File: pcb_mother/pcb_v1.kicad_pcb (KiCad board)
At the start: 2 copper layers, 90 x 70.2 mm, 27 parts, among them J1 Conn_01x02, J10 Conn_01x02, J11 Conn_01x06, J14 Conn_01x06, J2 Conn_01x03, J3 Conn_01x02, J4 Conn_01x02_Male, J5 Conn_01x02_Male, J9 Conn_01x02, Q10 2N2219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

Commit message: falta agregar el plano de tierra y los aujeros, comprobar todo. Ver tutoriales de tutoelectro (el gallego)
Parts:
- moved REF** 121.2 mm to (196.7, 39.1)
- moved REF** 83.5 mm to (185.2, 137.7)
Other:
- board size 90 x 70.2 mm -> 80 x 90 mm
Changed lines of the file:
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@@
     (links 104)
     (no_connects 0)
-    (area 68.724999 51.924999 158.875001 122.275001)
+    (area 72.632999 32.841 210.279286 136.365619)
     (thickness 1.6)
-    (drawings 3)
+    (drawings 6)
     (tracks 398)
     (zones 0)
@@
   )
   (module Mounting_Holes:MountingHole_4mm (layer F.Cu)
-    (at 77.6605 61.976)
+    (at 196.723 39.116)
     (descr "Mounting Hole 4mm, no annular")
     (tags "mounting hole 4mm no annular")
@@
   )
   (module Mounting_Holes:MountingHole_4mm (layer F.Cu)
-    (at 202.565 56.007)
+    (at 185.166 137.668)
     (descr "Mounting Hole 4mm, no annular")
     (tags "mounting hole 4mm no annular")
@@
     )
   )
+  (gr_line (start 65 50) (end 65 140) (angle 90) (layer Edge.Cuts) (width 0.15))
+  (gr_line (start 145 50) (end 65 50) (angle 90) (layer Edge.Cuts) (width 0.15))
+  (gr_line (start 145 140) (end 145 50) (angle 90) (layer Edge.Cuts) (width 0.15))
+  (gr_line (start 65 140) (end 145 140) (angle 90) (layer Edge.Cuts) (width 0.15))
+  (dimension 82.550391 (width 0.3) (layer F.Fab)
+    (gr_text "82,550 mm" (at 185.039 96.266 270.1762941) (layer F.Fab)
+      (effects (font (size 1.5 1.5) (thickness 0.3)))
+    )
+    (feature1 (pts (xy 185.166 137.541) (xy 185.166 137.541)))
+    (feature2 (pts (xy 184.912 54.991) (xy 184.912 54.991)))
+    (crossbar (pts (xy 184.912 54.991) (xy 185.166 137.541)))
+    (arrow1a (pts (xy 185.166 137.541) (xy 184.576116 136.416306)))
+    (arrow1b (pts (xy 185.166 137.541) (xy 185.748952 136.412697)))
+    (arrow2a (pts (xy 184.912 54.991) (xy 184.329048 56.119303)))
+    (arrow2b (pts (xy 184.912 54.991) (xy 185.501884 56.115694)))
+  )
   (gr_line (start 91.601 103.098) (end 91.401 103.098) (angle 90) (layer Edge.Cuts) (width 0.15))
-  (gr_line (start 158.8 52) (end 68.8 52) (angle 90) (layer Edge.Cuts) (width 0.15))
-  (gr_line (start 158.8 122.2) (end 158.8 52) (angle 90) (layer Edge.Cuts) (width 0.15))
   (segment (start 128.524 112.903) (end 128.524 109.601) (width 0.8) (layer F.Cu) (net 4))
   (segment (start 117.348 98.425) (end 117.348 97.028) (width 0.8) (layer F.Cu) (net 4))
@@
   (segment (start 102.12 81.776) (end 102.108 81.788) (width 0.8) (layer F.Cu) (net 8))
   (segment (start 102.12 81.776) (end 102.108 81.788) (width 0.8) (layer F.Cu) (net 8))
-  (segment (start 99.568 81.788) (end 99.568 82.804) (width 0.8) (layer F.Cu) (net 9) (status C00000))
-  (segment (start 99.568 82.804) (end 98.298 84.074) (width 0.8) (layer F.Cu) (net 9) (status 400000))
-  (segment (start 112.28 74.688) (end 112.28 76.24) (width 0.8) (layer F.Cu) (net 9) (status 800000))
+  (segment (start 99.568 81.788) (end 99.568 82.804) (width 0.8) (layer F.Cu) (net 9))
+  (segment (start 99.568 82.804) (end 98.298 84.074) (width 0.8) (layer F.Cu) (net 9))
+  (segment (start 112.28 74.688) (end 112.28 76.24) (width 0.8) (layer F.Cu) (net 9))
   (segment (start 108.712 71.12) (end 112.28 74.688) (width 0.8) (layer F.Cu) (net 9))
   (segment (start 86.868 71.12) (end 108.712 71.12) (width 0.8) (layer F.Cu) (net 9))
@@
   (segment (start 97.04 81.776) (end 97.028 81.788) (width 0.8) (layer F.Cu) (net 11))
   (segment (start 97.04 81.776) (end 97.028 81.788) (width 0.8) (layer F.Cu) (net 11))
-  (segment (start 107.569 131.318) (end 107.569 132.334) (width 0.8) (layer F.Cu) (net 12) (status 400000))
+  (segment (start 107.569 131.318) (end 107.569 132.334) (width 0.8) (layer F.Cu) (net 12))
   (segment (start 133.731 123.063) (end 133.731 105.283) (width 0.8) (layer F.Cu) (net 12))
   (segment (start 122.936 133.858) (end 133.731 123.063) (width 0.8) (layer F.Cu) (net 12))
@@
   (segment (start 132.6 65.8) (end 132.6 65.6) (width 0.8) (layer F.Cu) (net 12))
   (segment (start 133.7 75.3) (end 133.6 75.2) (width 0.8) (layer F.Cu) (net 12))
-  (segment (start 91.948 81.788) (end 89.154 81.788) (width 0.8) (layer F.Cu) (net 13) (status 400000))
-  (segment (start 96.647 72.517) (end 99.58 75.45) (width 0.8) (layer F.Cu) (net 13) (status 800000))
+  (segment (start 91.948 81.788) (end 89.154 81.788) (width 0.8) (layer F.Cu) (net 13))
+  (segment (start 96.647 72.517) (end 99.58 75.45) (width 0.8) (layer F.Cu) (net 13))
   (segment (start 87.503 72.517) (end 96.647 72.517) (width 0.8) (layer F.Cu) (net 13))
   (segment (start 84.455 75.565) (end 87.503 72.517) (width 0.8) (layer F.Cu) (net 13))
   (segment (start 84.455 77.089) (end 84.455 75.565) (width 0.8) (layer F.Cu) (net 13))
   (segment (start 89.154 81.788) (end 84.455 77.089) (width 0.8) (layer F.Cu) (net 13))
-  (segment (start 99.58 75.45) (end 99.58 76.24) (width 0.8) (layer F.Cu) (net 13) (status C00000))
+  (segment (start 99.58 75.45) (end 99.58 76.24) (width 0.8) (layer F.Cu) (net 13))
   (segment (start 99.58 76.24) (end 99.58 75.38) (width 0.8) (layer F.Cu) (net 13))
   (segment (start 99.58 76.24) (end 99.58 75.98) (width 0.8) (layer F.Cu) (net 13))
@@
   (segment (start 112.268 82.423) (end 112.268 81.788) (width 0.8) (layer F.Cu) (net 36))
   (segment (start 112.268 81.788) (end 112.268 82.169) (width 0.8) (layer F.Cu) (net 36))
-  (segment (start 106.426 109.093) (end 106.807 109.093) (width 0.8) (layer F.Cu) (net 37) (status C00000))
-  (segment (start 106.807 109.093) (end 108.585 107.315) (width 0.8) (layer F.Cu) (net 37) (status 400000))
-  (segment (start 104.648 101.092) (end 104.648 97.028) (width 0.8) (layer F.Cu) (net 37) (status 800000))
+  (segment (start 106.426 109.093) (end 106.807 109.093) (width 0.8) (layer F.Cu) (net 37))
+  (segment (start 106.807 109.093) (end 108.585 107.315) (width 0.8) (layer F.Cu) (net 37))
+  (segment (start 104.648 101.092) (end 104.648 97.028) (width 0.8) (layer F.Cu) (net 37))
   (segment (start 105.41 101.854) (end 104.648 101.092) (width 0.8) (layer F.Cu) (net 37))
   (segment (start 107.188 101.854) (end 105.41 101.854) (width 0.8) (layer F.Cu) (net 37))
@@
   (segment (start 102.108 97.028) (end 102.108 98.171) (width 0.8) (layer F.Cu) (net 38))
   (segment (start 102.108 97.028) (end 102.108 96.908) (width 0.8) (layer F.Cu) (net 38))
-  (segment (start 94.5 76.24) (end 86.574 76.24) (width 0.8) (layer F.Cu) (net 39) (status 400000))
+  (segment (start 94.5 76.24) (end 86.574 76.24) (width 0.8) (layer F.Cu) (net 39))
   (segment (start 86.36 76.454) (end 86.36 83.566) (width 0.8) (layer B.Cu) (net 39))
   (segment (start 86.487 76.327) (end 86.36 76.454) (width 0.8) (layer B.Cu) (net 39))
@@
   (via (at 86.36 98.298) (size 2) (drill 0.75) (layers F.Cu B.Cu) (net 39))
   (segment (start 89.154 101.092) (end 86.36 98.298) (width 0.8) (layer B.Cu) (net 39))
-  (segment (start 114.046 104.013) (end 114.046 103.886) (width 0.8) (layer F.Cu) (net 39) (status C00000))
-  (segment (start 114.046 103.886) (end 111.252 101.092) (width 0.8) (layer F.Cu) (net 39) (status 400000))
+  (segment (start 114.046 104.013) (end 114.046 103.886) (width 0.8) (layer F.Cu) (net 39))
+  (segment (start 114.046 103.886) (end 111.252 101.092) (width 0.8) (layer F.Cu) (net 39))
   (segment (start 100.33 103.378) (end 100.203 103.378) (width 0.8) (layer F.Cu) (net 39))
   (segment (start 102.616 101.092) (end 100.33 103.378) (width 0.8) (layer F.Cu) (net 39))
@@
   (segment (start 111.252 101.092) (end 102.616 101.092) (width 0.8) (layer B.Cu) (net 39))
   (via (at 111.252 101.092) (size 2) (drill 0.75) (layers F.Cu B.Cu) (net 39))
-  (segment (start 124.079 100.203) (end 124.079 101.346) (width 0.8) (layer F.Cu) (net 39) (status C00000))
-  (segment (start 124.079 101.346) (end 132.08 109.347) (width 0.8) (layer F.Cu) (net 39) (status 400000))
-  (segment (start 123.571 131.318) (end 110.109 131.318) (width 0.8) (layer F.Cu) (net 39) (status 800000))
+  (segment (start 124.079 100.203) (end 124.079 101.346) (width 0.8) (layer F.Cu) (net 39))
+  (segment (start 124.079 101.346) (end 132.08 109.347) (width 0.8) (layer F.Cu) (net 39))
+  (segment (start 123.571 131.318) (end 110.109 131.318) (width 0.8) (layer F.Cu) (net 39))
   (segment (start 132.08 122.809) (end 123.571 131.318) (width 0.8) (layer F.Cu) (net 39))
   (segment (start 132.08 109.347) (end 132.08 122.809) (width 0.8) (layer F.Cu) (net 39))
@@
   (segment (start 101.727 103.378) (end 101.727 103.378) (width 0.8) (layer F.Cu) (net 39))
   (segment (start 122.301 127.762) (end 123.825 127.762) (width 0.8) (layer F.Cu) (net 40))
-  (segment (start 119.888 99.06) (end 119.888 97.028) (width 0.8) (layer F.Cu) (net 40) (status 800000))
+  (segment (start 119.888 99.06) (end 119.888 97.028) (width 0.8) (layer F.Cu) (net 40))
   (segment (start 130.683 109.855) (end 119.888 99.06) (width 0.8) (layer F.Cu) (net 40))
   (segment (start 130.683 120.904) (end 130.683 109.855) (width 0.8) (layer F.Cu) (net 40))
@@
   (segment (start 77.089 104.14) (end 77.216 104.14) (width 0.8) (layer F.Cu) (net 43))
   (segment (start 117.348 81.788) (end 117.348 82.169) (width 0.8) (layer F.Cu) (net 43))
-  (segment (start 107.188 97.028) (end 107.188 99.949) (width 0.8) (layer F.Cu) (net 44) (status 400000))
-  (segment (start 109.982 111.633) (end 107.442 114.173) (width 0.8) (layer F.Cu) (net 44) (status 800000))
+  (segment (start 107.188 97.028) (end 107.188 99.949) (width 0.8) (layer F.Cu) (net 44))
+  (segment (start 109.982 111.633) (end 107.442 114.173) (width 0.8) (layer F.Cu) (net 44))
   (segment (start 109.982 102.743) (end 109.982 111.633) (width 0.8) (layer F.Cu) (net 44))
   (segment (start 107.188 99.949) (end 109.982 102.743) (width 0.8) (layer F.Cu) (net 44))
-  (segment (start 107.442 114.173) (end 106.426 114.173) (width 0.8) (layer F.Cu) (net 44) (status C00000))
+  (segment (start 107.442 114.173) (end 106.426 114.173) (width 0.8) (layer F.Cu) (net 44))
   (segment (start 106.426 114.173) (end 106.807 114.173) (width 0.8) (layer F.Cu) (net 44))
   (segment (start 112.268 97.028) (end 112.268 97.409) (width 0.8) (layer F.Cu) (net 45))

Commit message: se realiza un ultimo chekeo antes de la imprecion.
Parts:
- removed the REF** at (196.7, 39.1)
- added REF**: MountingHole_4mm, Mounting_Holes:MountingHole_4mm, F.Cu at (137.4, 131.3)
- added REF**: MountingHole_4mm, Mounting_Holes:MountingHole_4mm, F.Cu at (137.4, 61.3)
- D1: footprint Diodes_SMD:D_1206 -> Diodes_THT:D_DO-35_SOD27_P7.62mm_Horizontal
- moved REF** 112.9 mm to (72.4, 131.3)
- moved REF** 112.7 mm to (72.4, 61.3)
- moved D1 7.27 mm to (136.1, 110.5), turned to 90 degrees
- moved J5 0.30 mm to (84.0, 56.3)
- moved C4 0.20 mm to (88.9, 56.4)
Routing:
- net /Vcc_bat: track 135.0 -> 135.6 mm
- net Net-(D1-Pad2): track 3.69 -> 3.11 mm
- added copper zone on F.Cu, net GND

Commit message: Version final impresa
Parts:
- moved J11 0.92 mm to (110.1, 128.7)
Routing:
- net VCC: track 230.5 -> 233.0 mm
- net /L5_a: track 11.2 -> 12.4 mm
- net /L2_a: track 16.8 -> 17.8 mm
- net /L1_a: track 21.6 -> 22.6 mm
- net /L3_a: track 24.4 -> 25.4 mm
- net /L4_a: track 18.3 -> 19.2 mm

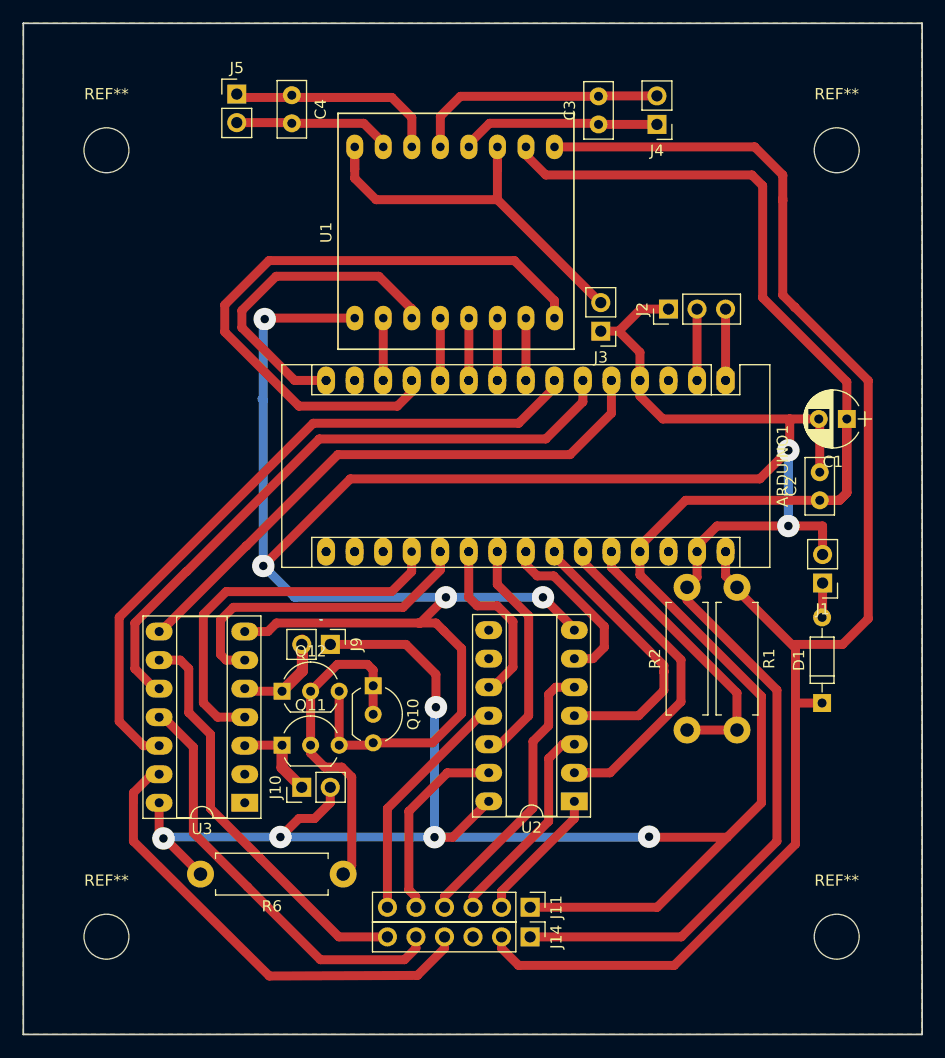
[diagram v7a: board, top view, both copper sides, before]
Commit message: Se modificaron los margenes para que sea igual o a penas mas grande (+2mm). Esta version SI se imprimio, la anterior no, porque era muy grande.
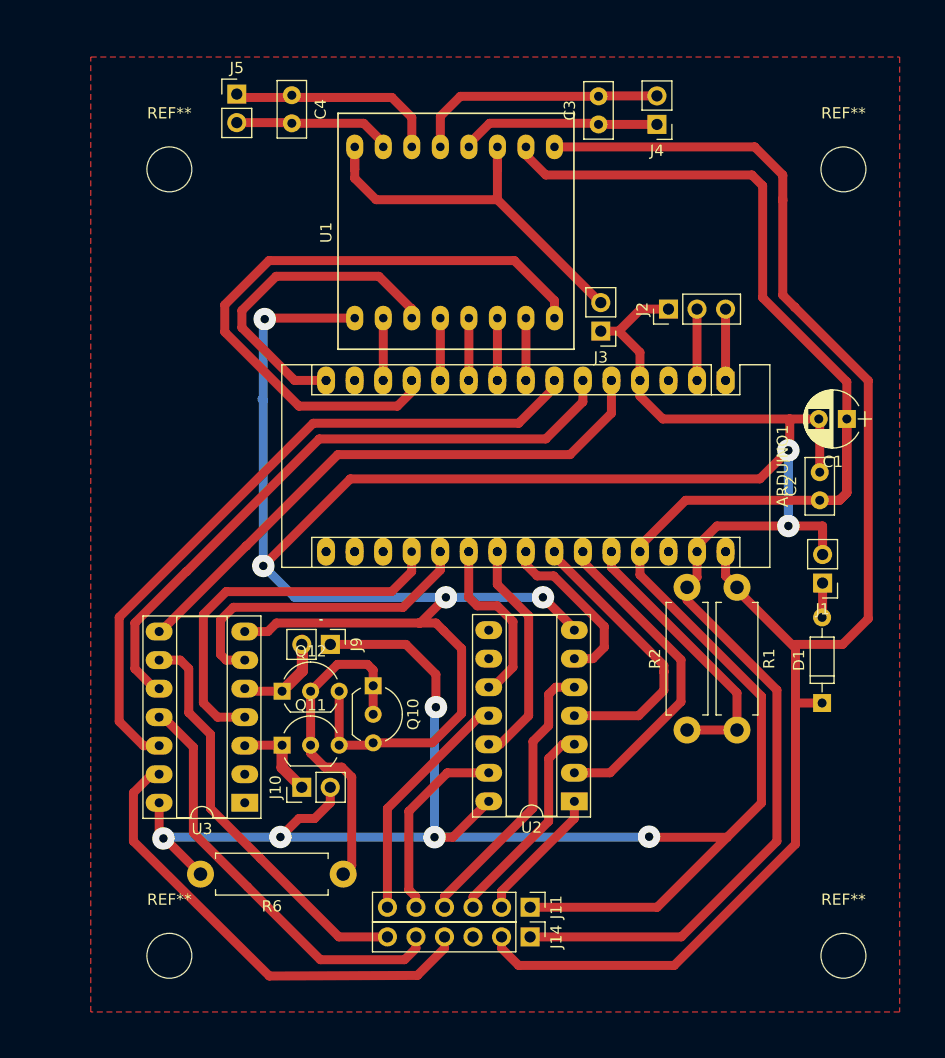
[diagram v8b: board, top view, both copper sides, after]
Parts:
- moved REF** 5.85 mm to (78.0, 63.0)
- moved REF** 5.85 mm to (78.0, 133.0)
- moved REF** 1.80 mm to (138.0, 63.0)
- moved REF** 1.80 mm to (138.0, 133.0)
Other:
- board outline removed
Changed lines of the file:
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@@
     (links 104)
     (no_connects 0)
-    (area 64.685714 27.3 172.85 140.075001)
+    (area 70.285714 43.3 170.85 149.700001)
     (thickness 1.6)
-    (drawings 7)
+    (drawings 14)
     (tracks 417)
     (zones 0)
@@
   )
   (module Mounting_Holes:MountingHole_4mm (layer F.Cu)
-    (at 137.4 131.3)
+    (at 138 133)
     (descr "Mounting Hole 4mm, no annular")
     (tags "mounting hole 4mm no annular")
@@
   )
   (module Mounting_Holes:MountingHole_4mm (layer F.Cu)
-    (at 137.4 61.3)
+    (at 138 63)
     (descr "Mounting Hole 4mm, no annular")
     (tags "mounting hole 4mm no annular")
@@
   )
   (module Mounting_Holes:MountingHole_4mm (layer F.Cu)
-    (at 72.4 61.3)
+    (at 78 63)
     (descr "Mounting Hole 4mm, no annular")
     (tags "mounting hole 4mm no annular")
@@
   )
   (module Mounting_Holes:MountingHole_4mm (layer F.Cu)
-    (at 72.4 131.3)
+    (at 78 133)
     (descr "Mounting Hole 4mm, no annular")
     (tags "mounting hole 4mm no annular")
@@
     )
   )
-  (dimension 80 (width 0.3) (layer F.Fab)
-    (gr_text "80,000 mm" (at 105 28.65) (layer F.Fab)
+  (dimension 72 (width 0.3) (layer F.CrtYd)
+    (gr_text "72,000 mm" (at 107 156.35) (layer F.CrtYd)
       (effects (font (size 1.5 1.5) (thickness 0.3)))
     )
-    (feature1 (pts (xy 65 50) (xy 65 27.3)))
-    (feature2 (pts (xy 145 50) (xy 145 27.3)))
-    (crossbar (pts (xy 145 30) (xy 65 30)))
-    (arrow1a (pts (xy 65 30) (xy 66.126504 29.413579)))
-    (arrow1b (pts (xy 65 30) (xy 66.126504 30.586421)))
-    (arrow2a (pts (xy 145 30) (xy 143.873496 29.413579)))
-    (arrow2b (pts (xy 145 30) (xy 143.873496 30.586421)))
-  )
-  (dimension 90 (width 0.3) (layer F.Fab)
-    (gr_text "90,000 mm" (at 166.35 95 270) (layer F.Fab)
+    (feature1 (pts (xy 143 138) (xy 143 157.7)))
+    (feature2 (pts (xy 71 138) (xy 71 157.7)))
+    (crossbar (pts (xy 71 155) (xy 143 155)))
+    (arrow1a (pts (xy 143 155) (xy 141.873496 155.586421)))
+    (arrow1b (pts (xy 143 155) (xy 141.873496 154.413579)))
+    (arrow2a (pts (xy 71 155) (xy 72.126504 155.586421)))
+    (arrow2b (pts (xy 71 155) (xy 72.126504 154.413579)))
+  )
+  (dimension 85 (width 0.3) (layer Dwgs.User)
+    (gr_text "85,000 mm" (at 164.35 95.5 90) (layer Dwgs.User)
       (effects (font (size 1.5 1.5) (thickness 0.3)))
     )
-    (feature1 (pts (xy 145 140) (xy 167.7 140)))
-    (feature2 (pts (xy 145 50) (xy 167.7 50)))
-    (crossbar (pts (xy 165 50) (xy 165 140)))
-    (arrow1a (pts (xy 165 140) (xy 164.413579 138.873496)))
-    (arrow1b (pts (xy 165 140) (xy 165.586421 138.873496)))
-    (arrow2a (pts (xy 165 50) (xy 164.413579 51.126504)))
-    (arrow2b (pts (xy 165 50) (xy 165.586421 51.126504)))
-  )
-  (gr_line (start 65 50) (end 65 140) (angle 90) (layer Edge.Cuts) (width 0.15))
-  (gr_line (start 145 50) (end 65 50) (angle 90) (layer Edge.Cuts) (width 0.15))
-  (gr_line (start 145 140) (end 145 50) (angle 90) (layer Edge.Cuts) (width 0.15))
-  (gr_line (start 65 140) (end 145 140) (angle 90) (layer Edge.Cuts) (width 0.15))
+    (feature1 (pts (xy 143 53) (xy 165.7 53)))
+    (feature2 (pts (xy 143 138) (xy 165.7 138)))
+    (crossbar (pts (xy 163 138) (xy 163 53)))
+    (arrow1a (pts (xy 163 53) (xy 163.586421 54.126504)))
+    (arrow1b (pts (xy 163 53) (xy 162.413579 54.126504)))
+    (arrow2a (pts (xy 163 138) (xy 163.586421 136.873496)))
+    (arrow2b (pts (xy 163 138) (xy 162.413579 136.873496)))
+  )
+  (dimension 60 (width 0.3) (layer Dwgs.User)
+    (gr_text "60,000 mm" (at 108 148.35) (layer Dwgs.User)
+      (effects (font (size 1.5 1.5) (thickness 0.3)))
+    )
+    (feature1 (pts (xy 138 133) (xy 138 149.7)))
+    (feature2 (pts (xy 78 133) (xy 78 149.7)))
+    (crossbar (pts (xy 78 147) (xy 138 147)))
+    (arrow1a (pts (xy 138 147) (xy 136.873496 147.586421)))
+    (arrow1b (pts (xy 138 147) (xy 136.873496 146.413579)))
+    (arrow2a (pts (xy 78 147) (xy 79.126504 147.586421)))
+    (arrow2b (pts (xy 78 147) (xy 79.126504 146.413579)))
+  )
+  (dimension 70 (width 0.3) (layer Dwgs.User)
+    (gr_text "70,000 mm" (at 157.35 98 270) (layer Dwgs.User)
+      (effects (font (size 1.5 1.5) (thickness 0.3)))
+    )
+    (feature1 (pts (xy 138 133) (xy 158.7 133)))
+    (feature2 (pts (xy 138 63) (xy 158.7 63)))
+    (crossbar (pts (xy 156 63) (xy 156 133)))
+    (arrow1a (pts (xy 156 133) (xy 155.413579 131.873496)))
+    (arrow1b (pts (xy 156 133) (xy 156.586421 131.873496)))
+    (arrow2a (pts (xy 156 63) (xy 155.413579 64.126504)))
+    (arrow2b (pts (xy 156 63) (xy 156.586421 64.126504)))
+  )
+  (gr_line (start 71 138) (end 71 53) (angle 90) (layer F.Fab) (width 0.2))
+  (gr_line (start 143 138) (end 71 138) (angle 90) (layer F.Fab) (width 0.2))
+  (gr_line (start 143 53) (end 143 138) (angle 90) (layer F.Fab) (width 0.2))
+  (gr_line (start 71 53) (end 143 53) (angle 90) (layer F.Fab) (width 0.2))
+  (gr_line (start 143 53) (end 142 53) (angle 90) (layer F.Fab) (width 0.2))
+  (gr_line (start 143 103) (end 143 53) (angle 90) (layer F.Fab) (width 0.2))
+  (gr_line (start 71 107) (end 71 53) (angle 90) (layer F.Fab) (width 0.2))
+  (gr_line (start 71 107) (end 71 138) (angle 90) (layer F.Fab) (width 0.2))
+  (gr_line (start 143 103) (end 143 138) (angle 90) (layer F.Fab) (width 0.2))
   (gr_line (start 91.601 103.098) (end 91.401 103.098) (angle 90) (layer Edge.Cuts) (width 0.15))
   (segment (start 128.524 112.903) (end 128.524 109.601) (width 0.8) (layer F.Cu) (net 4))
@@
   (segment (start 115.189 116.713) (end 114.046 116.713) (width 0.8) (layer F.Cu) (net 46))
   (zone (net 39) (net_name GND) (layer F.Cu) (hatch edge 0.508)
-    (connect_pads (clearance 0.508))
+    (connect_pads thru_hole_only (clearance 0.508))
     (min_thickness 0.4)
-    (fill yes (arc_segments 16) (thermal_gap 0.508) (thermal_bridge_width 0.508) (smoothing fillet) (radius 2))
+    (fill yes (arc_segments 16) (thermal_gap 0.508) (thermal_bridge_width 0.508))
     (polygon
       (pts
-        (xy 145 140) (xy 65 140) (xy 65 50) (xy 145 50)
+        (xy 143 138) (xy 71 138) (xy 71 53) (xy 143 53)
       )
     )
